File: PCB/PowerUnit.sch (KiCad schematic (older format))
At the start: 135 parts, among them J1 MX150-20, J2 MX150-20, J3 MX150-8, J4 REDCUBE, J5 REDFIT-4, Q1 BC847C, Q10 STD45P4LLF6AG, Q11 STD45P4LLF6AG, Q12 STD15P6F6AG, Q13 STD15P6F6AG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

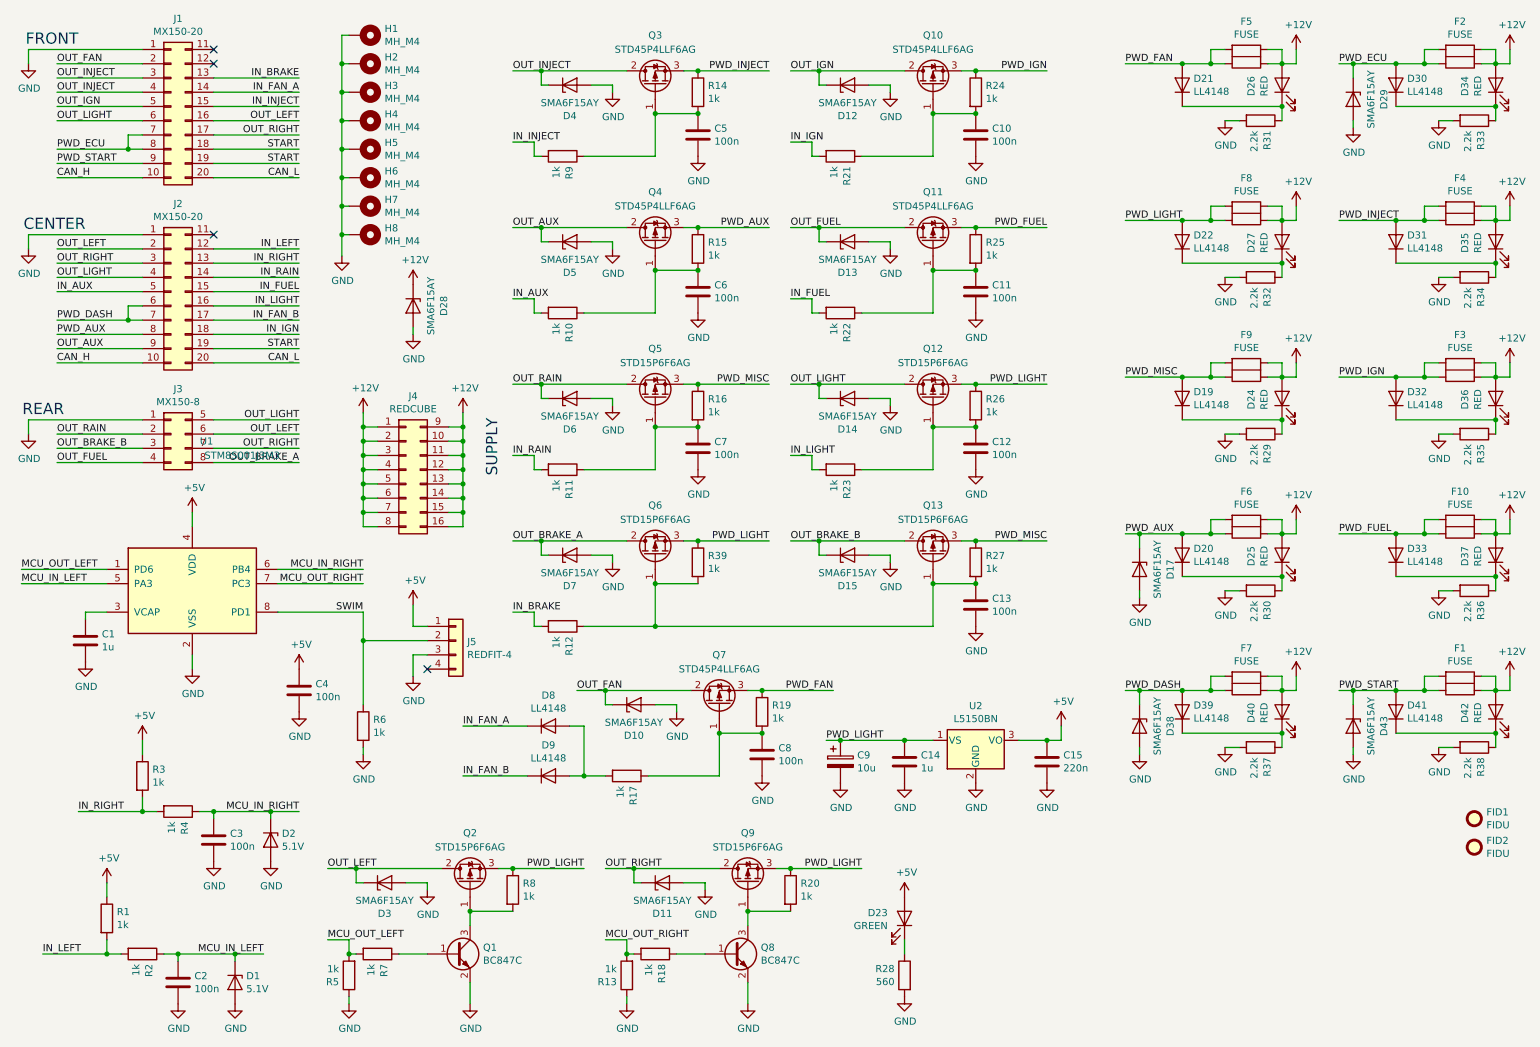
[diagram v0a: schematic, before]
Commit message: new high-side switch and debugconn
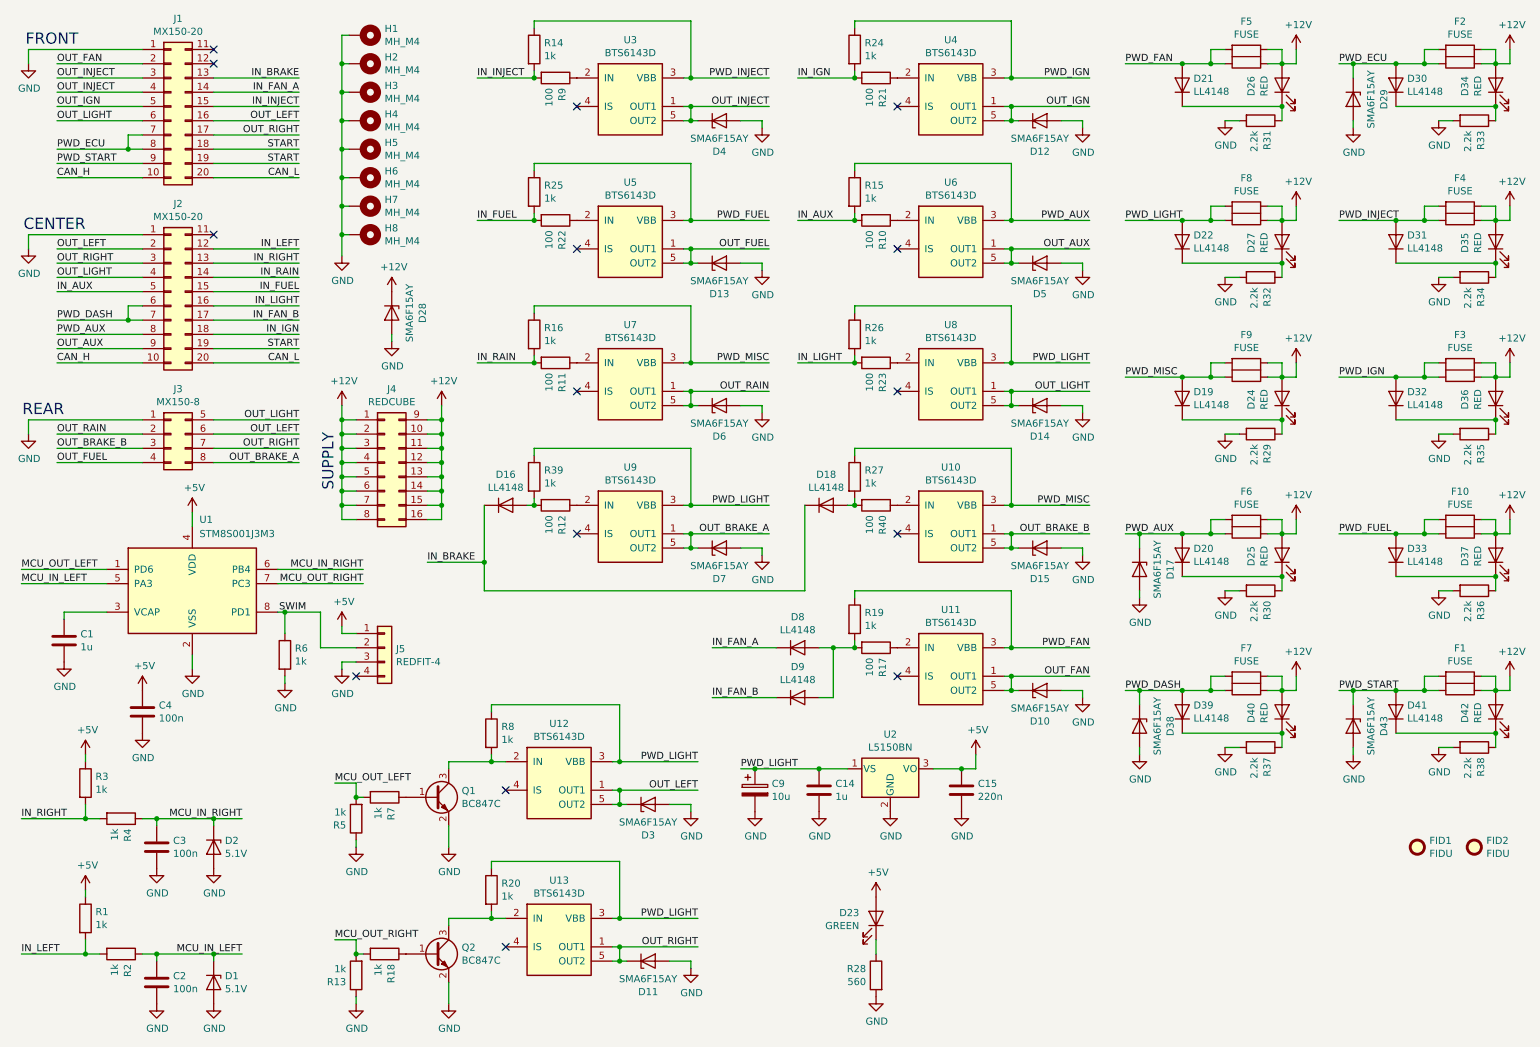
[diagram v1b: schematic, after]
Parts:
- removed C10, C11, C12, C13, C5, C6, C7, C8: 100n, erp:C_0805_2012Metric, symbol erp:C
- removed Q10, Q11, Q3, Q4, Q7: STD45P4LLF6AG, erp:TO-252-3_TabPin2, symbol erp:Q_PMOS_GDS
- removed Q12, Q13, Q2, Q5, Q6, Q9: STD15P6F6AG, erp:TO-252-3_TabPin2, symbol erp:Q_PMOS_GDS
- removed Q8: BC847C, erp:SOT-23, symbol erp:Q_NPN_BEC
- added D16, D18: LL4148, erp:D_MiniMELF, symbol erp:D
- added Q2: BC847C, erp:SOT-23, symbol erp:Q_NPN_BEC
- added R40: 100, erp:R_0805_2012Metric, symbol erp:R
- added U10, U11, U12, U13, U3, U4, U5, U6, U7, U8, U9: BTS6143D, erp:TO-252-5_TabPin3, symbol erp:BTS61x
- J5: footprint (none) -> erp:Wurth_WR-WST_IDC_4
- R10, R11, R12, R17, R21, R22, R23, R9: value 1k -> 100; ItemNo 200750 -> 200700
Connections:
- net GND: now also Q2.2 (E)
- net IN_AUX: now also R15.2
- net IN_BRAKE: now also D16.1 (K), D18.1 (K); no longer R12.2
- net IN_FUEL: now also R25.2
- net IN_IGN: now also R24.2
- net IN_INJECT: now also R14.2
- net IN_LIGHT: now also R26.2
- net IN_RAIN: now also R16.2
- net OUT_AUX: now also U6.1 (OUT1), U6.5 (OUT2)
- net OUT_BRAKE_A: now also U9.1 (OUT1), U9.5 (OUT2)
- net OUT_BRAKE_B: now also U10.1 (OUT1), U10.5 (OUT2)
- net OUT_FAN: now also U11.1 (OUT1), U11.5 (OUT2)
- net OUT_FUEL: now also U5.1 (OUT1), U5.5 (OUT2)
- net OUT_IGN: now also U4.1 (OUT1), U4.5 (OUT2)
- net OUT_INJECT: now also U3.1 (OUT1), U3.5 (OUT2)
- net OUT_LEFT: now also U12.1 (OUT1), U12.5 (OUT2)
- net OUT_LIGHT: now also U8.1 (OUT1), U8.5 (OUT2)
- net OUT_RAIN: now also U7.1 (OUT1), U7.5 (OUT2)
- net OUT_RIGHT: now also U13.1 (OUT1), U13.5 (OUT2)
- net PWD_AUX: now also U6.3 (VBB)
- net PWD_FAN: now also U11.3 (VBB)
- net PWD_FUEL: now also U5.3 (VBB)
- net PWD_IGN: now also U4.3 (VBB)
- net PWD_INJECT: now also U3.3 (VBB)
- net PWD_LIGHT: now also U12.3 (VBB), U13.3 (VBB), U8.3 (VBB), U9.3 (VBB)
- net PWD_MISC: now also U10.3 (VBB), U7.3 (VBB)
- net at R21.1: now also U4.2 (IN); no longer R24.2
- net at R20.2: now also Q2.3 (C), U13.2 (IN)
- net at R18.1: now also Q2.1 (B)
- net at Q1.3 (C), R8.2: now also U12.2 (IN)
- net at R9.1: now also U3.2 (IN); no longer R14.2
- net at R22.1: now also U5.2 (IN); no longer R25.2
- net at R10.1: now also U6.2 (IN); no longer R15.2
- net at R23.1: now also U8.2 (IN); no longer R26.2
- net at R19.2: now also D8.2 (A), D9.2 (A), R17.2; no longer R17.1
- net at R11.1: now also U7.2 (IN); no longer R16.2
- new net: R12.1, U9.2 (IN)
- new net: D16.2 (A), R12.2, R39.2
- new net: R40.1, U10.2 (IN)
- new net: D18.2 (A), R27.2, R40.2
- new net: R17.1, U11.2 (IN)
- no-connect marks 4 -> 15
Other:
- moved on the sheet: C1, C14, C15, C2, C3, C4, C9, D1, D2, D23, D28, D4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

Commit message: remove resistors / New layout
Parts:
- removed R14, R15, R16, R19, R20, R24, R25, R26, R27, R39, R8: 1k, erp:R_0805_2012Metric, symbol erp:R
- U10, U11, U12, U13, U3, U4, U5, U6, U7, U8, U9: footprint erp:TO-252-5_TabPin3 -> erp:TO-252-5_TabPin3X
